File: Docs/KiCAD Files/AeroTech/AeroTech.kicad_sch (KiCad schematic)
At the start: 22 parts, among them J1 Power Input, J2 SSR FAN, J3 WATER PUMP, J4 Water Level, J5 Water Level, J6 Water Level, J7 SOLAR PANEL, J8 PH Sensor, J9 TDS Sensor, Q5 BC817, Q6 AO3401A, U1 ESP32-DevKitC, U2 L7805

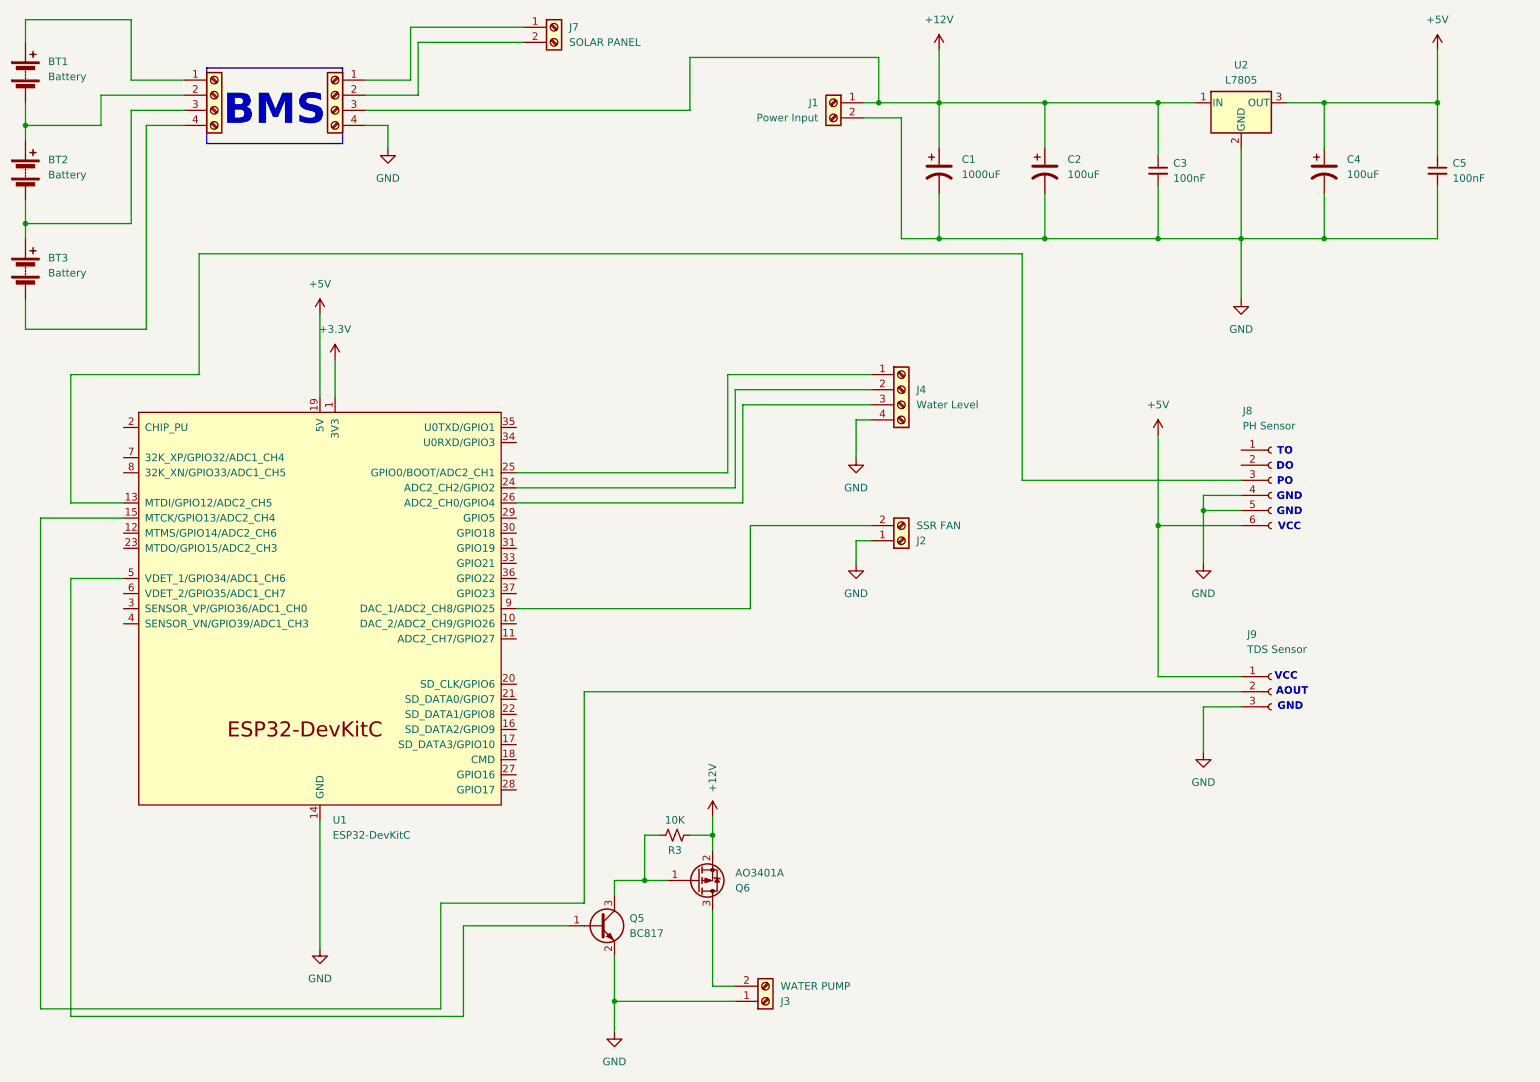
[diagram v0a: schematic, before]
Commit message: added TFT screen to the full schematic (KiCAD and jpg)
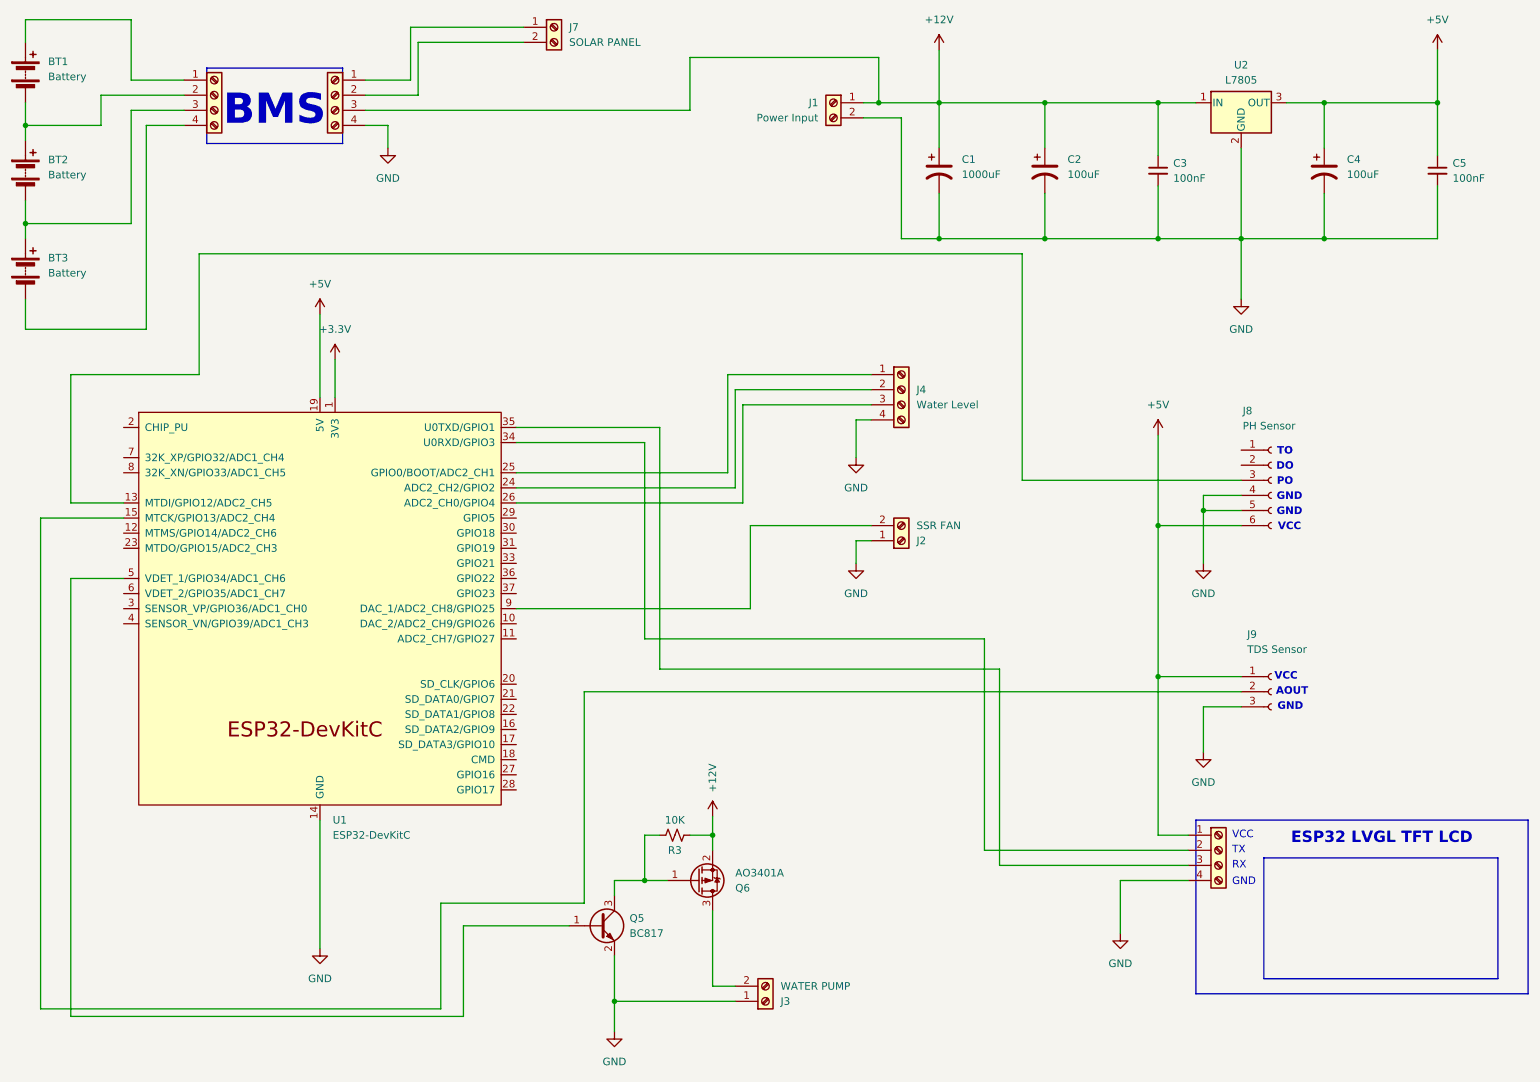
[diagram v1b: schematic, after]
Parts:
- added J10: Coin Acceptor, symbol Connector:Screw_Terminal_01x04
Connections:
- net +5V: now also J10.1 (Pin_1)
- net GND: now also J10.4 (Pin_4)
- net at U1.34 (U0RXD/GPIO3): now also J10.2 (Pin_2)
- net at U1.35 (U0TXD/GPIO1): now also J10.3 (Pin_3)
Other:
- note added: "ESP32 LVGL TFT LCD"
- note added: "RX"
- note added: "TX"
